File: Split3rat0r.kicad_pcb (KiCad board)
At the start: 2 copper layers, 75 parts, among them J1 Conn_01x20, K1 KEYSW, K10 KEYSW, K11 KEYSW, K12 KEYSW, K13 KEYSW, K14 KEYSW, K15 KEYSW, K16 KEYSW, K17 KEYSW, K18 KEYSW, K19 KEYSW, K2 KEYSW, K20 KEYSW, K21 KEYSW, K22 KEYSW, K23 KEYSW, K24 KEYSW, K25 KEYSW, K26 KEYSW, K27 KEYSW, K28 KEYSW, K29 KEYSW, K3 KEYSW, K30 KEYSW, K4 KEYSW, K5 KEYSW, K6 KEYSW, K7 KEYSW, K8 KEYSW, K9 KEYSW, U1 TEENSY2.0

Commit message: Added rotary acoder switch + pcb layout progress
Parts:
- added SW1: Rotary_Encoder_Switch, Rotary_Encoder:RotaryEncoder_Alps_EC11E-Switch_Vertical_H20mm, F.Cu at (170.5, 140.7)
- D1, D10, D11, D12, D13, D14, D15, D16, D17, D18, D19, D2, D20, D21, D22, D23, D24, D25, D26, D27, D28, D29, D3, D30, D4, D5, D6, D7, D8, D9, LD1, LD2, LD3, R1, R2, R3, U1: moved to F.Cu
- moved H5 173.8 mm to (52.4, 23.8)
- moved H4 150.5 mm to (166.7, 23.8)
- moved U1 143.8 mm to (179.8, 55.3), turned to 270 degrees
- moved D13 112.4 mm to (63.7, 48.6), turned to 270 degrees
- moved D19 110.2 mm to (67.5, 50.5), turned to 270 degrees
- moved D30 102.3 mm to (166.4, 52.4), turned to 270 degrees
- moved H2 99.4 mm to (71.4, 95.2)
- moved J1 98.0 mm to (172.0, 124.3)
- moved D1 84.9 mm to (56.1, 44.9), turned to 270 degrees
- moved D29 84.6 mm to (147.3, 52.5), turned to 270 degrees
- moved LD1 82.3 mm to (172.0, 87.9), turned to 270 degrees
- moved LD2 79.9 mm to (179.7, 88.1), turned to 270 degrees
- moved D20 79.5 mm to (86.6, 50.6), turned to 270 degrees
- moved LD3 78.9 mm to (187.5, 88.2), turned to 270 degrees
- moved D24 73.5 mm to (162.6, 50.6), turned to 270 degrees
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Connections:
- U1 pad 21: Net-(U1-Pad21) -> /row6
- U1 pad 22: Net-(U1-Pad22) -> /encB
- U1 pad 6: Net-(U1-Pad6) -> /encA

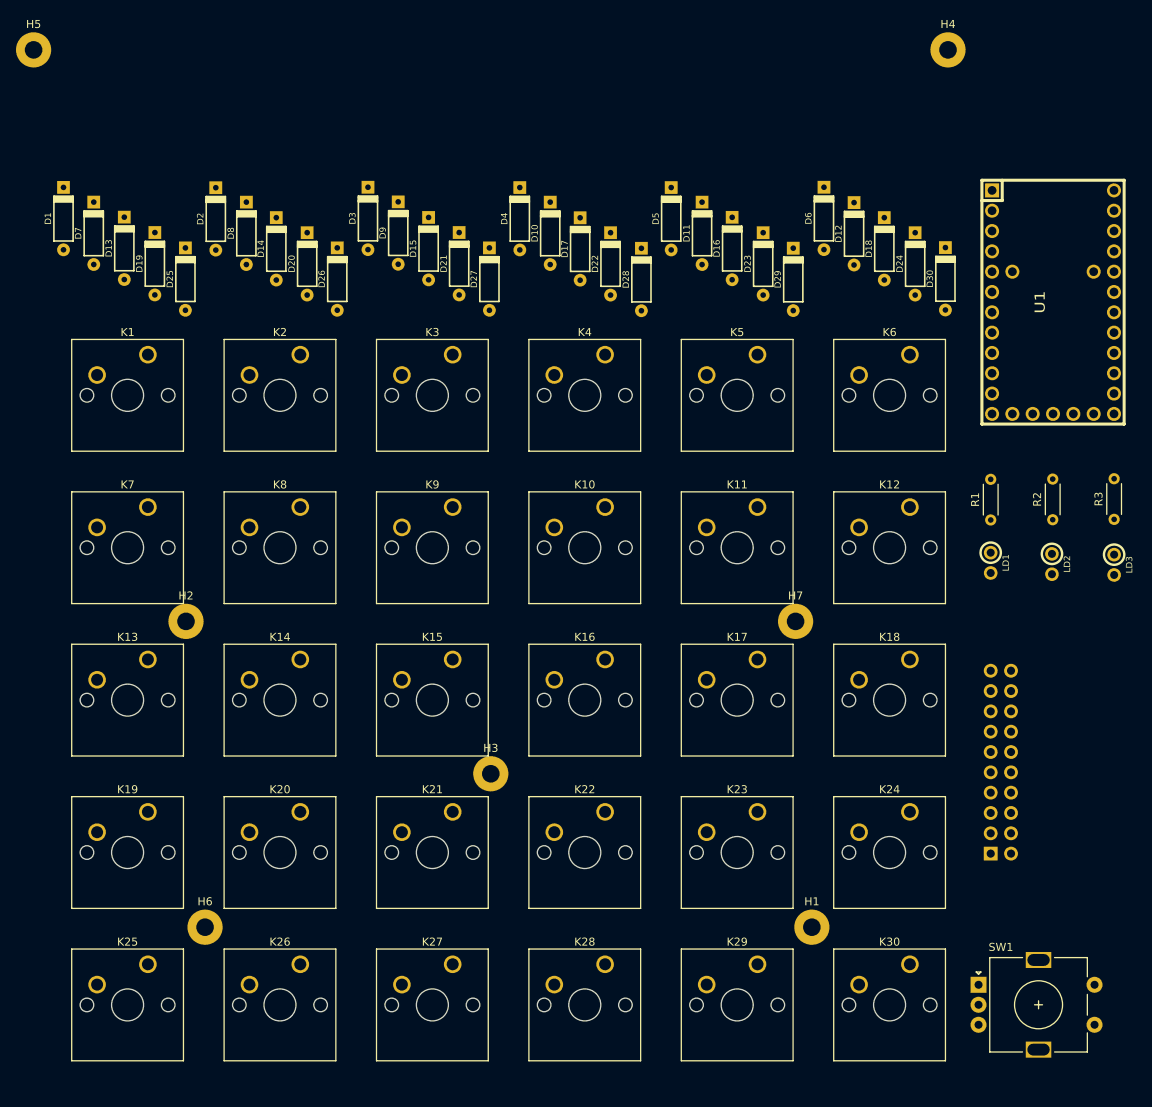
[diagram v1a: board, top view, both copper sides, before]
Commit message: mounting holes + edge cuts done
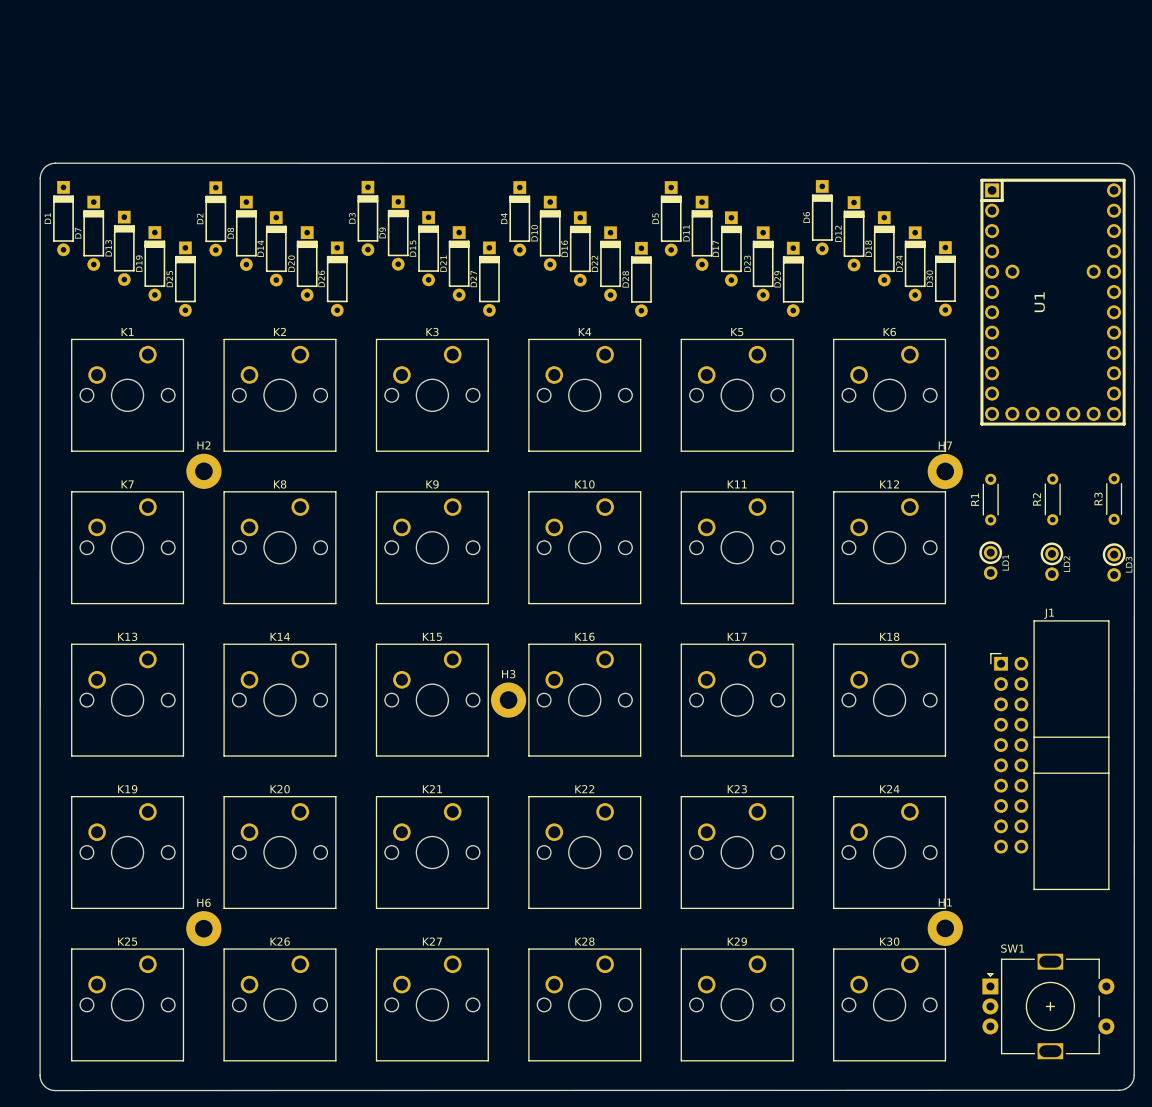
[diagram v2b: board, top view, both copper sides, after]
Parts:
- removed H4, H5: MountingHole, MountingHole:MountingHole_2.2mm_M2_Pad
- J1: moved to F.Cu
- moved H7 26.5 mm to (166.3, 76.5)
- moved J1 23.8 mm to (173.3, 100.5)
- moved D16 19.0 mm to (120.7, 48.7)
- moved D17 18.9 mm to (139.6, 48.7)
- moved H2 18.9 mm to (73.7, 76.5)
- moved H1 16.7 mm to (166.3, 133.6)
- moved H3 9.47 mm to (111.8, 105.1)
- moved SW1 1.50 mm to (172.0, 140.9)
- moved H6 0.24 mm to (73.7, 133.7)
- moved D6 0.23 mm to (151.0, 44.8)
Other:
- board outline added: 136.8 x 115.9 mm
